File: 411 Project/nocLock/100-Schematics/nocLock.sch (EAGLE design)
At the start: 7 parts, among them U1 ATMEGA88A

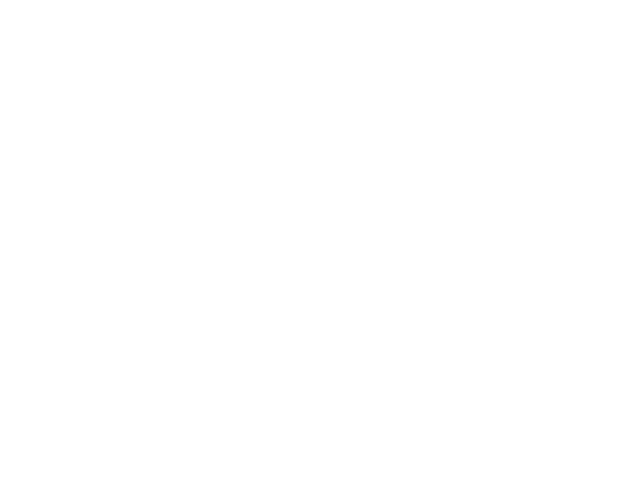
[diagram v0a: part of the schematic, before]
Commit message: added more components to library.
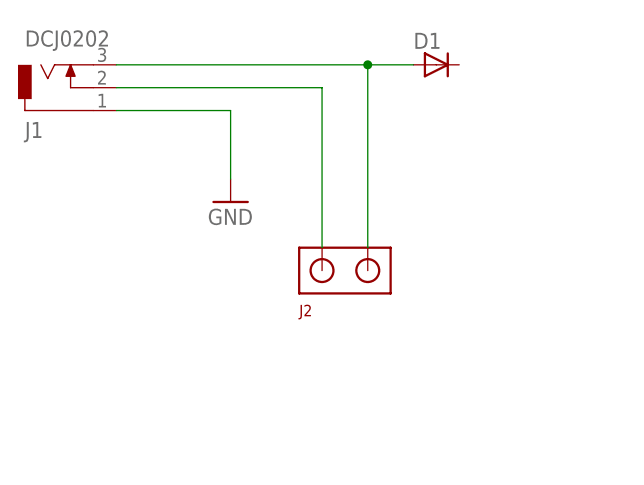
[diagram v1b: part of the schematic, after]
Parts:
- added D1: (no value), semicon-smd-ipc:D-SMB
- added J1: DCJ0202, con-jack:DCJ0202
- added J2: (no value), nocLock:JST-[S2B-PH-K-S(LF)(SN)]
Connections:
- new net GND: J1.1
- new net N$2: D1.A, J1.3
- new net N$3: J1.2
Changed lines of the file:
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@@
 <part name="SUPPLY7" library="supply2" deviceset="GND" device=""/>
 <part name="U1" library="nocLock" deviceset="ATMEGA88A" device=""/>
+<part name="J1" library="con-jack" deviceset="DCJ0202" device=""/>
+<part name="D1" library="semicon-smd-ipc" deviceset="D-" device="SMB"/>
+<part name="GND1" library="supply1" deviceset="GND" device=""/>
+<part name="J2" library="nocLock" deviceset="JST-[S2B-PH-K-S(LF)(SN)]" device=""/>
 </parts>
 <sheets>
@@
 <instance part="SUPPLY7" gate="GND" x="124.46" y="165.1"/>
 <instance part="U1" gate="G$1" x="210.82" y="182.88"/>
+<instance part="J1" gate="G$1" x="93.98" y="287.02" rot="MR180"/>
+<instance part="D1" gate="G$1" x="137.16" y="289.56"/>
+<instance part="GND1" gate="1" x="114.3" y="274.32"/>
+<instance part="J2" gate="G$1" x="127" y="266.7"/>
 </instances>
 <busses>
 </busses>
 <nets>
+<net name="GND" class="0">
+<segment>
+<pinref part="J1" gate="G$1" pin="1"/>
+<wire x1="101.6" y1="284.48" x2="114.3" y2="284.48" width="0.1524" layer="91"/>
+<wire x1="114.3" y1="284.48" x2="114.3" y2="276.86" width="0.1524" layer="91"/>
+<pinref part="GND1" gate="1" pin="GND"/>
+</segment>
+</net>
+<net name="N$2" class="0">
+<segment>
+<pinref part="J1" gate="G$1" pin="3"/>
+<pinref part="D1" gate="G$1" pin="A"/>
+<wire x1="101.6" y1="289.56" x2="129.54" y2="289.56" width="0.1524" layer="91"/>
+<wire x1="129.54" y1="289.56" x2="134.62" y2="289.56" width="0.1524" layer="91"/>
+<wire x1="129.54" y1="269.24" x2="129.54" y2="289.56" width="0.1524" layer="91"/>
+<junction x="129.54" y="289.56"/>
+</segment>
+</net>
+<net name="N$3" class="0">
+<segment>
+<pinref part="J1" gate="G$1" pin="2"/>
+<wire x1="101.6" y1="287.02" x2="124.46" y2="287.02" width="0.1524" layer="91"/>
+<wire x1="124.46" y1="269.24" x2="124.46" y2="287.02" width="0.1524" layer="91"/>
+</segment>
+</net>
 </nets>
 </sheet>
